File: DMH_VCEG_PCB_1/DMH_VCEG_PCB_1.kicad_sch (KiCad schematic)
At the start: 0 parts

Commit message: Placed Circuit B pages
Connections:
- no-connect marks 10 -> 0
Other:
- added sheet Core Circuit B (Core_Circuit_B.kicad_sch)
- added sheet Extra Features B (Extra_Features_B.kicad_sch)

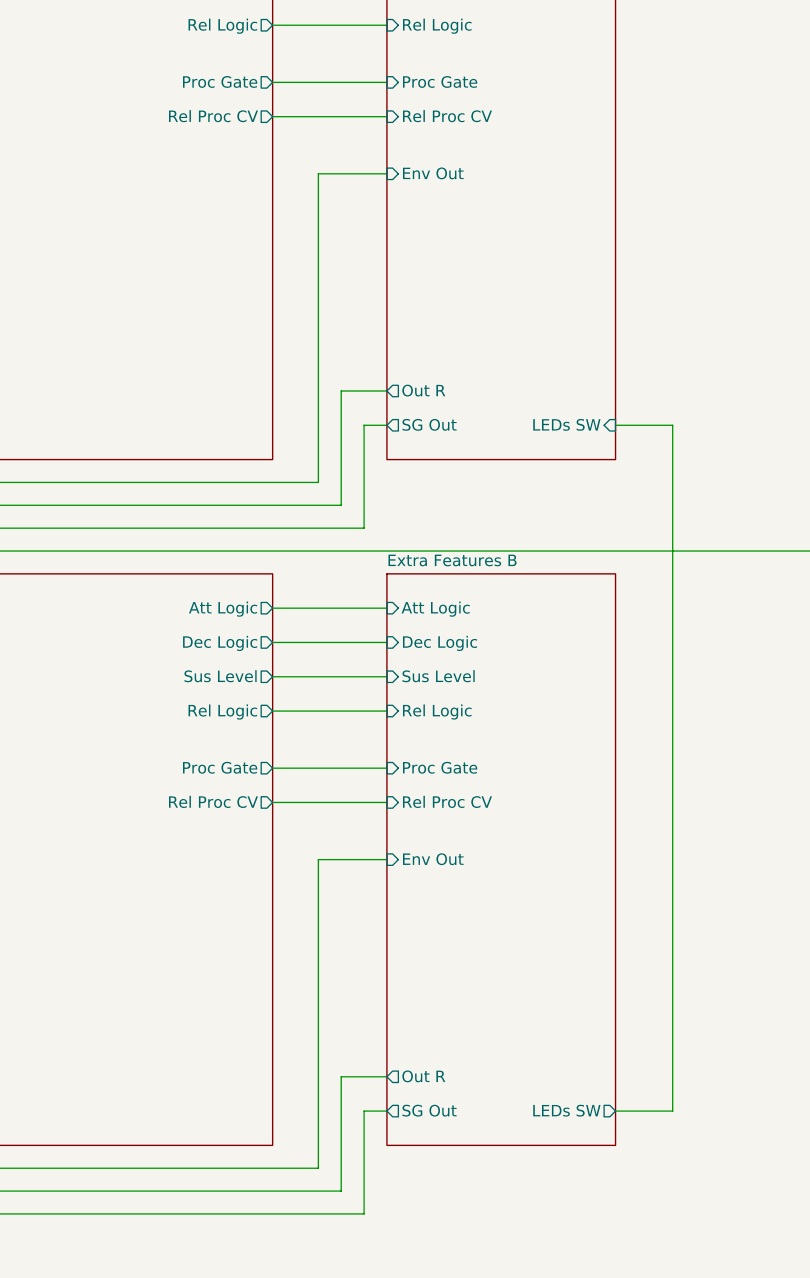
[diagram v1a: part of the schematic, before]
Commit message: Added Loop circuit
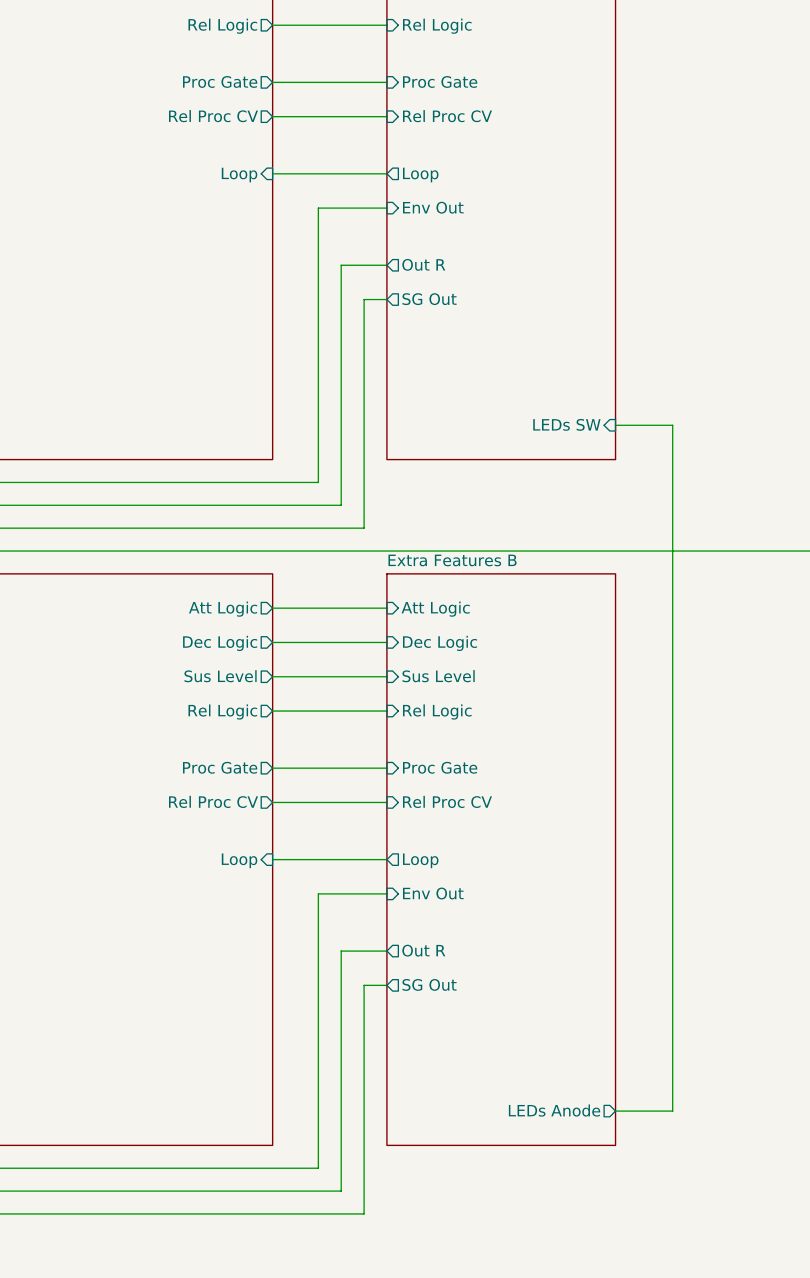
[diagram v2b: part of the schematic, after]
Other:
- sheet Core Circuit A ports: added Loop; removed none
- sheet Core Circuit B ports: added Loop; removed none
- sheet Extra Features A ports: added Loop; removed none
- sheet Extra Features B ports: added LEDs Anode, Loop; removed LEDs SW
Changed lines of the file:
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@@
 	(wire
 		(pts
-			(xy 162.56 96.52) (xy 162.56 85.09)
+			(xy 162.56 96.52) (xy 162.56 71.12)
 		)
 		(stroke
@@
 	(wire
 		(pts
-			(xy 165.1 81.28) (xy 160.02 81.28)
+			(xy 165.1 67.31) (xy 160.02 67.31)
 		)
 		(stroke
@@
 	(wire
 		(pts
+			(xy 152.4 57.15) (xy 165.1 57.15)
+		)
+		(stroke
+			(width 0)
+			(type default)
+		)
+	)
+	(wire
+		(pts
 			(xy 38.1 144.78) (xy 27.94 144.78)
 		)
@@
 	(wire
 		(pts
+			(xy 152.4 133.35) (xy 165.1 133.35)
+		)
+		(stroke
+			(width 0)
+			(type default)
+		)
+	)
+	(wire
+		(pts
 			(xy 63.5 152.4) (xy 68.58 152.4)
 		)
@@
 	(wire
 		(pts
-			(xy 157.48 57.15) (xy 165.1 57.15)
+			(xy 157.48 60.96) (xy 165.1 60.96)
 		)
 		(stroke
@@
 	(wire
 		(pts
-			(xy 165.1 161.29) (xy 162.56 161.29)
+			(xy 165.1 147.32) (xy 162.56 147.32)
 		)
 		(stroke
@@
 	(wire
 		(pts
-			(xy 160.02 81.28) (xy 160.02 93.98)
-		)
-		(stroke
-			(width 0)
-			(type default)
-		)
-	)
-	(wire
-		(pts
-			(xy 165.1 133.35) (xy 157.48 133.35)
+			(xy 160.02 67.31) (xy 160.02 93.98)
+		)
+		(stroke
+			(width 0)
+			(type default)
+		)
+	)
+	(wire
+		(pts
+			(xy 165.1 137.16) (xy 157.48 137.16)
 		)
 		(stroke
@@
 	(wire
 		(pts
-			(xy 157.48 133.35) (xy 157.48 167.64)
+			(xy 157.48 137.16) (xy 157.48 167.64)
 		)
 		(stroke
@@
 	(wire
 		(pts
-			(xy 157.48 91.44) (xy 157.48 57.15)
+			(xy 157.48 91.44) (xy 157.48 60.96)
 		)
 		(stroke
@@
 	(wire
 		(pts
-			(xy 160.02 157.48) (xy 160.02 170.18)
+			(xy 160.02 143.51) (xy 160.02 170.18)
 		)
 		(stroke
@@
 	(wire
 		(pts
-			(xy 162.56 161.29) (xy 162.56 172.72)
+			(xy 162.56 147.32) (xy 162.56 172.72)
 		)
 		(stroke
@@
 	(wire
 		(pts
-			(xy 162.56 85.09) (xy 165.1 85.09)
+			(xy 162.56 71.12) (xy 165.1 71.12)
 		)
 		(stroke
@@
 	(wire
 		(pts
-			(xy 165.1 157.48) (xy 160.02 157.48)
+			(xy 165.1 143.51) (xy 160.02 143.51)
 		)
 		(stroke
@@
 			)
 		)
+		(pin "Loop" input
+			(at 152.4 133.35 0)
+			(effects
+				(font
+					(size 1.27 1.27)
+				)
+				(justify right)
+			)
+		)
 		(instances
 			(project "DMH_VCEG_PCB_1"
@@
 		)
 		(pin "Env Out" input
-			(at 165.1 133.35 180)
+			(at 165.1 137.16 180)
 			(effects
 				(font
@@
 		)
 		(pin "Out R" output
-			(at 165.1 157.48 180)
+			(at 165.1 143.51 180)
 			(effects
 				(font
@@
 		)
 		(pin "SG Out" output
-			(at 165.1 161.29 180)
+			(at 165.1 147.32 180)
 			(effects
 				(font
@@
 			)
 		)
-		(pin "LEDs SW" output
+		(pin "Loop" output
+			(at 165.1 133.35 180)
+			(effects
+				(font
+					(size 1.27 1.27)
+				)
+				(justify left)
+			)
+		)
+		(pin "LEDs Anode" output
 			(at 190.5 161.29 0)
 			(effects
@@
 			)
 		)
+		(pin "Loop" input
+			(at 152.4 57.15 0)
+			(effects
+				(font
+					(size 1.27 1.27)
+				)
+				(justify right)
+			)
+		)
 		(instances
 			(project "DMH_VCEG_PCB_1"
@@
 		)
 		(pin "Env Out" input
-			(at 165.1 57.15 180)
+			(at 165.1 60.96 180)
 			(effects
 				(font
@@
 		)
 		(pin "Out R" output
-			(at 165.1 81.28 180)
+			(at 165.1 67.31 180)
 			(effects
 				(font
@@
 		)
 		(pin "SG Out" output
-			(at 165.1 85.09 180)
+			(at 165.1 71.12 180)
 			(effects
 				(font
@@
 			)
 		)
+		(pin "Loop" output
+			(at 165.1 57.15 180)
+			(effects
+				(font
+					(size 1.27 1.27)
+				)
+				(justify left)
+			)
+		)

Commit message: Redesigned circuit A
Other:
- added sheet CV Processing A (CV_Processing_A.kicad_sch)
- sheet Core Circuit A ports: added Att Proc CV, Dec & /Sus, Dec Proc CV, Max Level; removed Att CV, Dec CV, Rel CV, Sus CV, Sus Level
- sheet Extra Features A ports: added Dec & /Sus, Sus Logic; removed SG Out

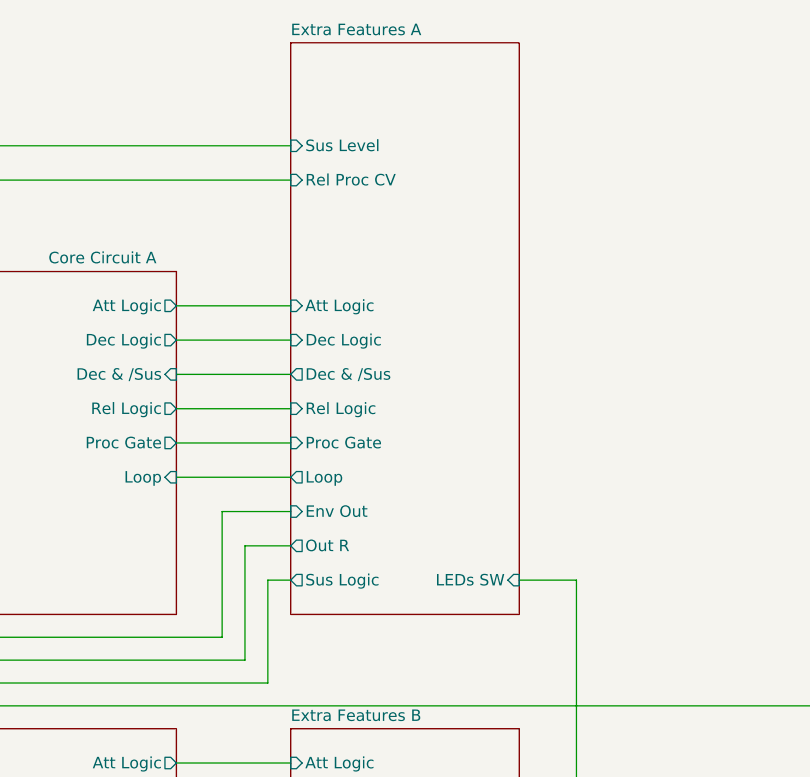
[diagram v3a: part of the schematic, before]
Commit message: Redesign A almost finished
Need to update the Out R to use Release Current Mirror
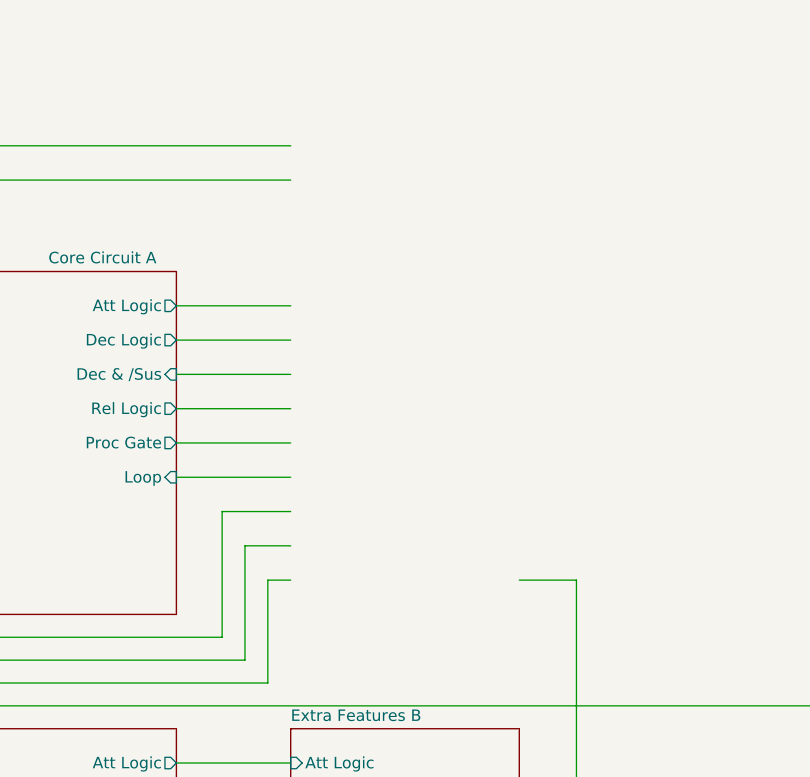
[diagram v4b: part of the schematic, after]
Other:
- removed sheet Extra Features A
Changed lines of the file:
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@@
-		)
-	)
-	(sheet
-		(at 165.1 25.4)
-		(size 25.4 63.5)
-		(exclude_from_sim no)
-		(in_bom yes)
-		(on_board yes)
-		(dnp no)
-		(fields_autoplaced yes)
-		(stroke
-			(width 0.1524)
-			(type solid)
-		)
-		(fill
-			(color 0 0 0 0.0000)
-		)
-		(property "Sheetname" "Extra Features A"
-			(at 165.1 24.6884 0)
-			(effects
-				(font
-					(size 1.27 1.27)
-				)
-				(justify left bottom)
-			)
-		)
-		(property "Sheetfile" "Extra_Features_A.kicad_sch"
-			(at 165.1 89.4846 0)
-			(effects
-				(font
-					(size 1.27 1.27)
-				)
-				(justify left top)
-				(hide yes)
-			)
-		)
-		(pin "Att Logic" input
-			(at 165.1 54.61 180)
-			(effects
-				(font
-					(size 1.27 1.27)
-				)
-				(justify left)
-			)
-		)
-		(pin "Dec Logic" input
-			(at 165.1 58.42 180)
-			(effects
-				(font
-					(size 1.27 1.27)
-				)
-				(justify left)
-			)
-		)
-		(pin "Env Out" input
-			(at 165.1 77.47 180)
-			(effects
-				(font
-					(size 1.27 1.27)
-				)
-				(justify left)
-			)
-		)
-		(pin "Out R" output
-			(at 165.1 81.28 180)
-			(effects
-				(font
-					(size 1.27 1.27)
-				)
-				(justify left)
-			)
-		)
-		(pin "Proc Gate" input
-			(at 165.1 69.85 180)
-			(effects
-				(font
-					(size 1.27 1.27)
-				)
-				(justify left)
-			)
-		)
-		(pin "Rel Logic" input
-			(at 165.1 66.04 180)
-			(effects
-				(font
-					(size 1.27 1.27)
-				)
-				(justify left)
-			)
-		)
-		(pin "Rel Proc CV" input
-			(at 165.1 40.64 180)
-			(effects
-				(font
-					(size 1.27 1.27)
-				)
-				(justify left)
-			)
-		)
-		(pin "Sus Level" input
-			(at 165.1 36.83 180)
-			(effects
-				(font
-					(size 1.27 1.27)
-				)
-				(justify left)
-			)
-		)
-		(pin "LEDs SW" input
-			(at 190.5 85.09 0)
-			(effects
-				(font
-					(size 1.27 1.27)
-				)
-				(justify right)
-			)
-		)
-		(pin "Loop" output
-			(at 165.1 73.66 180)
-			(effects
-				(font
-					(size 1.27 1.27)
-				)
-				(justify left)
-			)
-		)
-		(pin "Sus Logic" output
-			(at 165.1 85.09 180)
-			(effects
-				(font
-					(size 1.27 1.27)
-				)
-				(justify left)
-			)
-		)
-		(pin "Dec & {slash}Sus" output
-			(at 165.1 62.23 180)
-			(effects
-				(font
-					(size 1.27 1.27)
-				)
-				(justify left)
-			)
-		)
-		(instances
-			(project "DMH_VCEG_PCB_1"
-				(path "/58f4306d-5387-4983-bb08-41a2313fd315"
-					(page "8")
-				)
-			)
 		)
 	)

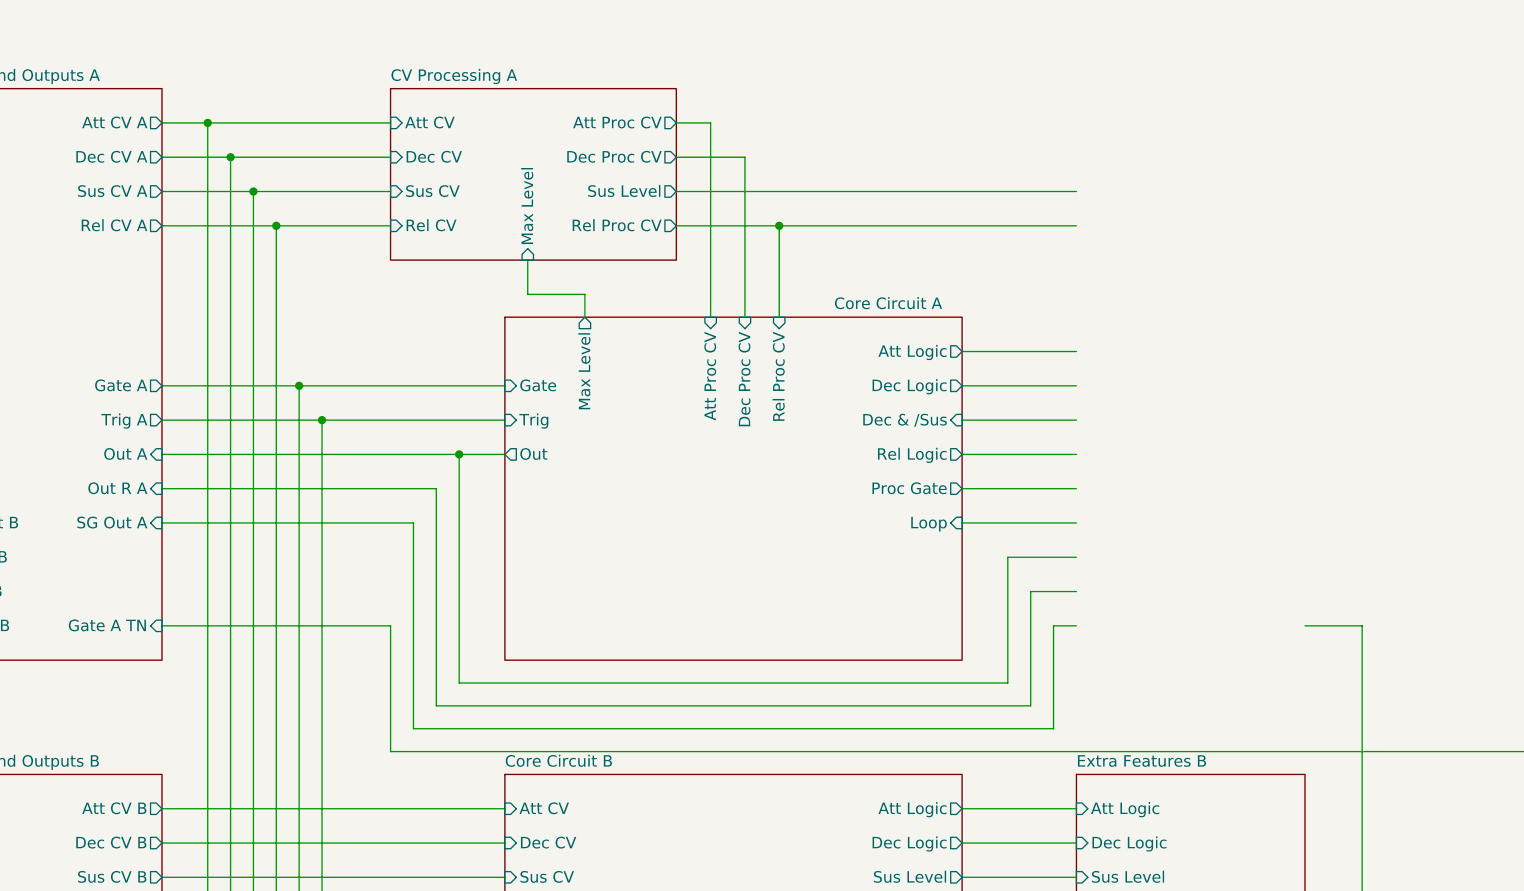
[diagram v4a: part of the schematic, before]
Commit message: Finished circuit A redesign
Except for component re-annotation
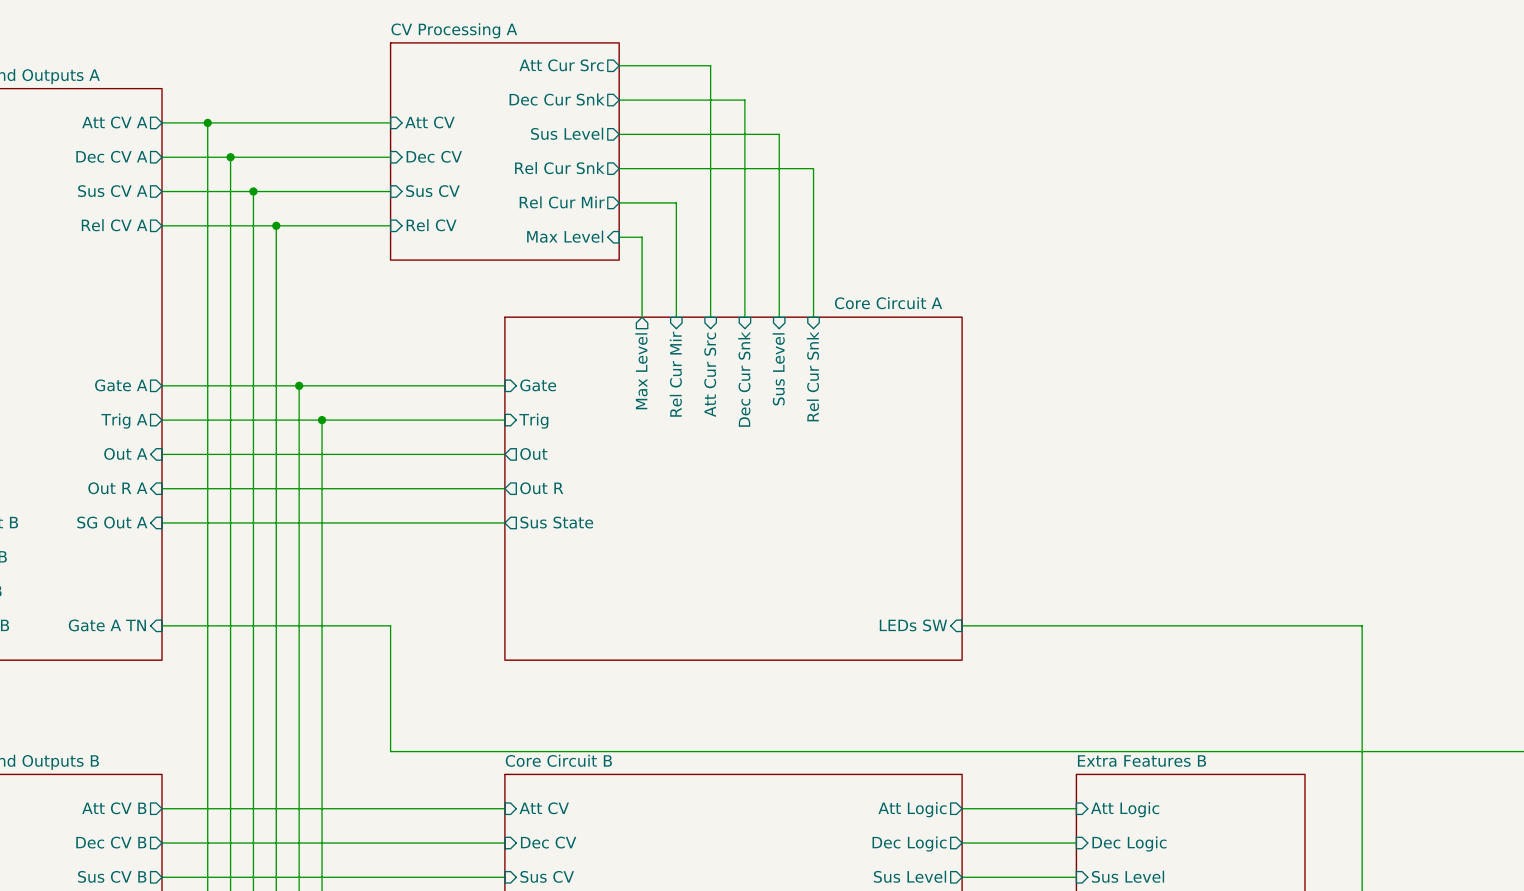
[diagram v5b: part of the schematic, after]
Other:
- sheet CV Processing A ports: added Att Cur Src, Dec Cur Snk, Rel Cur Mir, Rel Cur Snk; removed Att Proc CV, Dec Proc CV, Rel Proc CV
- sheet Core Circuit A ports: added Att Cur Src, Dec Cur Snk, LEDs SW, Out R, Rel Cur Mir, Rel Cur Snk, Sus Level, Sus State; removed Att Logic, Att Proc CV, Dec & /Sus, Dec Logic, Dec Proc CV, Loop, Proc Gate, Rel Logic, Rel Proc CV
